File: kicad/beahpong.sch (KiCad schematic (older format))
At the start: 16 parts, among them J1 Conn_02x20_Odd_Even, J2 Conn_01x02, J3 Screw_Terminal_01x02, Q1 DMG2305UX, U1 CAT24C32, U2 DMMT5401

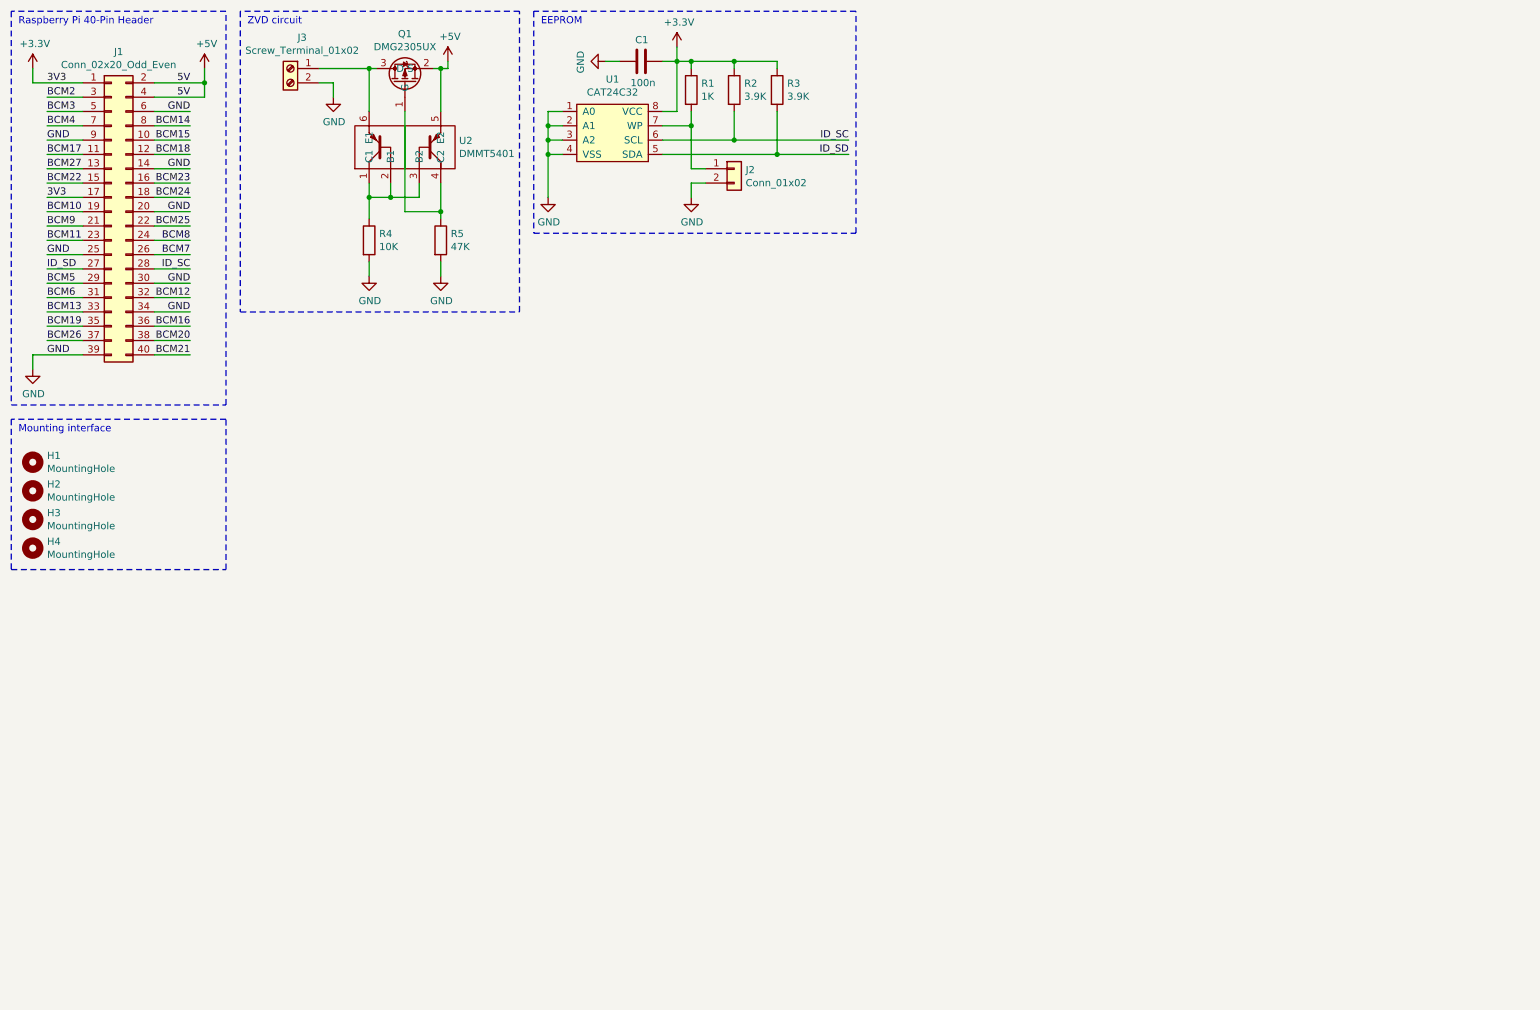
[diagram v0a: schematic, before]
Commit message: Add level shifters
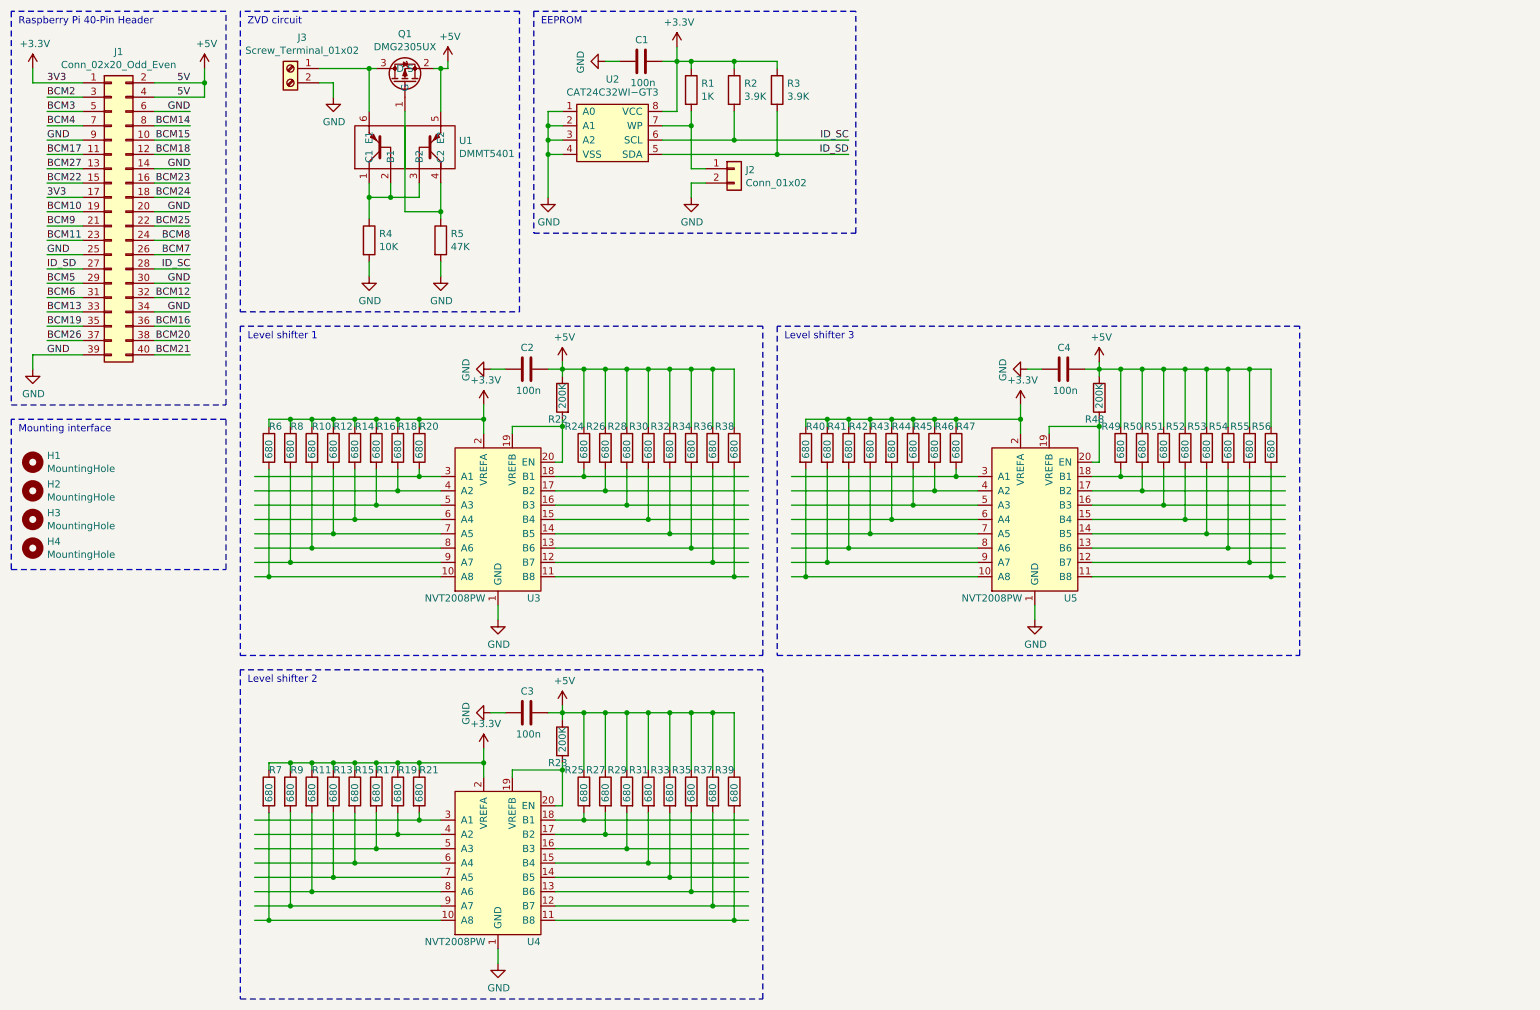
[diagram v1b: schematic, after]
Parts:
- removed U1: CAT24C32, Package_SO:SOIC-8_3.9x4.9mm_P1.27mm, symbol beahpong:CAT24C32
- removed U2: DMMT5401, Package_TO_SOT_SMD:SOT-23-6, symbol beahpong:DMMT5401
- added C2, C3, C4: 100n, Capacitor_SMD:C_0402_1005Metric, symbol Device:C
- added R10, R11, R12, R13, R14, R15, R16, R17, R18, R19, R20, R21, R24, R25, R26, R27, R28, R29, R30, R31, R32, R33, R34, R35, R36, R37, R38, R39, R40, R41, R42, R43, R44, R45, R46, R47, R49, R50, R51, R52, R53, R54, R55, R56, R6, R7, R8, R9: 680, Resistor_SMD:R_0603_1608Metric, symbol Device:R
- added R22, R23, R48: 200K, Resistor_SMD:R_0603_1608Metric, symbol Device:R
- added U1: DMMT5401, Package_TO_SOT_SMD:SOT-23-6, symbol beahpong:DMMT5401
- added U2: CAT24C32WI−GT3, Package_SO:SOIC-8_3.9x4.9mm_P1.27mm, symbol beahpong:CAT24C32WI−GT3
- added U3, U4, U5: NVT2008PW, Package_SO:TSSOP-20_4.4x6.5mm_P0.65mm, symbol beahpong:NVT2008PW
- J3: footprint Connector_Phoenix_MC:PhoenixContact_MCV_1,5_2-G-3.5_1x02_P3.50mm_Vertical -> Connector_Molex:Molex_KK-254_AE-6410-02A_1x02_P2.54mm_Vertical
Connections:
- wire segments 96 -> 372
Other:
- note added: "Level shifter 1"
- note added: "Level shifter 2"
- note added: "Level shifter 3"

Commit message: Finished layout of pcb
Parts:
- added J4, J5, J6, J7: Conn_01x03, Connector_PinHeader_2.54mm:PinHeader_1x03_P2.54mm_Vertical, symbol Connector_Generic:Conn_01x03
- added J8: Conn_02x12_Odd_Even, Connector_PinHeader_2.54mm:PinHeader_2x12_P2.54mm_Vertical, symbol Connector_Generic:Conn_02x12_Odd_Even
- J3: footprint Connector_Molex:Molex_KK-254_AE-6410-02A_1x02_P2.54mm_Vertical -> Connector_Phoenix_MC:PhoenixContact_MC_1,5_2-G-3.5_1x02_P3.50mm_Horizontal
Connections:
- net labels added: DOUT_M, DOUT_P1, DOUT_P2, RESERVED, SENSOR_P1_0, SENSOR_P1_1, SENSOR_P1_2, SENSOR_P1_3, SENSOR_P1_4, SENSOR_P1_5, SENSOR_P1_6, SENSOR_P1_7, SENSOR_P1_8, SENSOR_P1_9, SENSOR_P2_0, SENSOR_P2_1, SENSOR_P2_2, SENSOR_P2_3, SENSOR_P2_4, SENSOR_P2_5, SENSOR_P2_6, SENSOR_P2_7, SENSOR_P2_8, SENSOR_P2_9
- wire segments 372 -> 420
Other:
- note added: "Sensor header"
- note added: "WS2812B Headers"
- moved on the sheet: C2, C3, C4

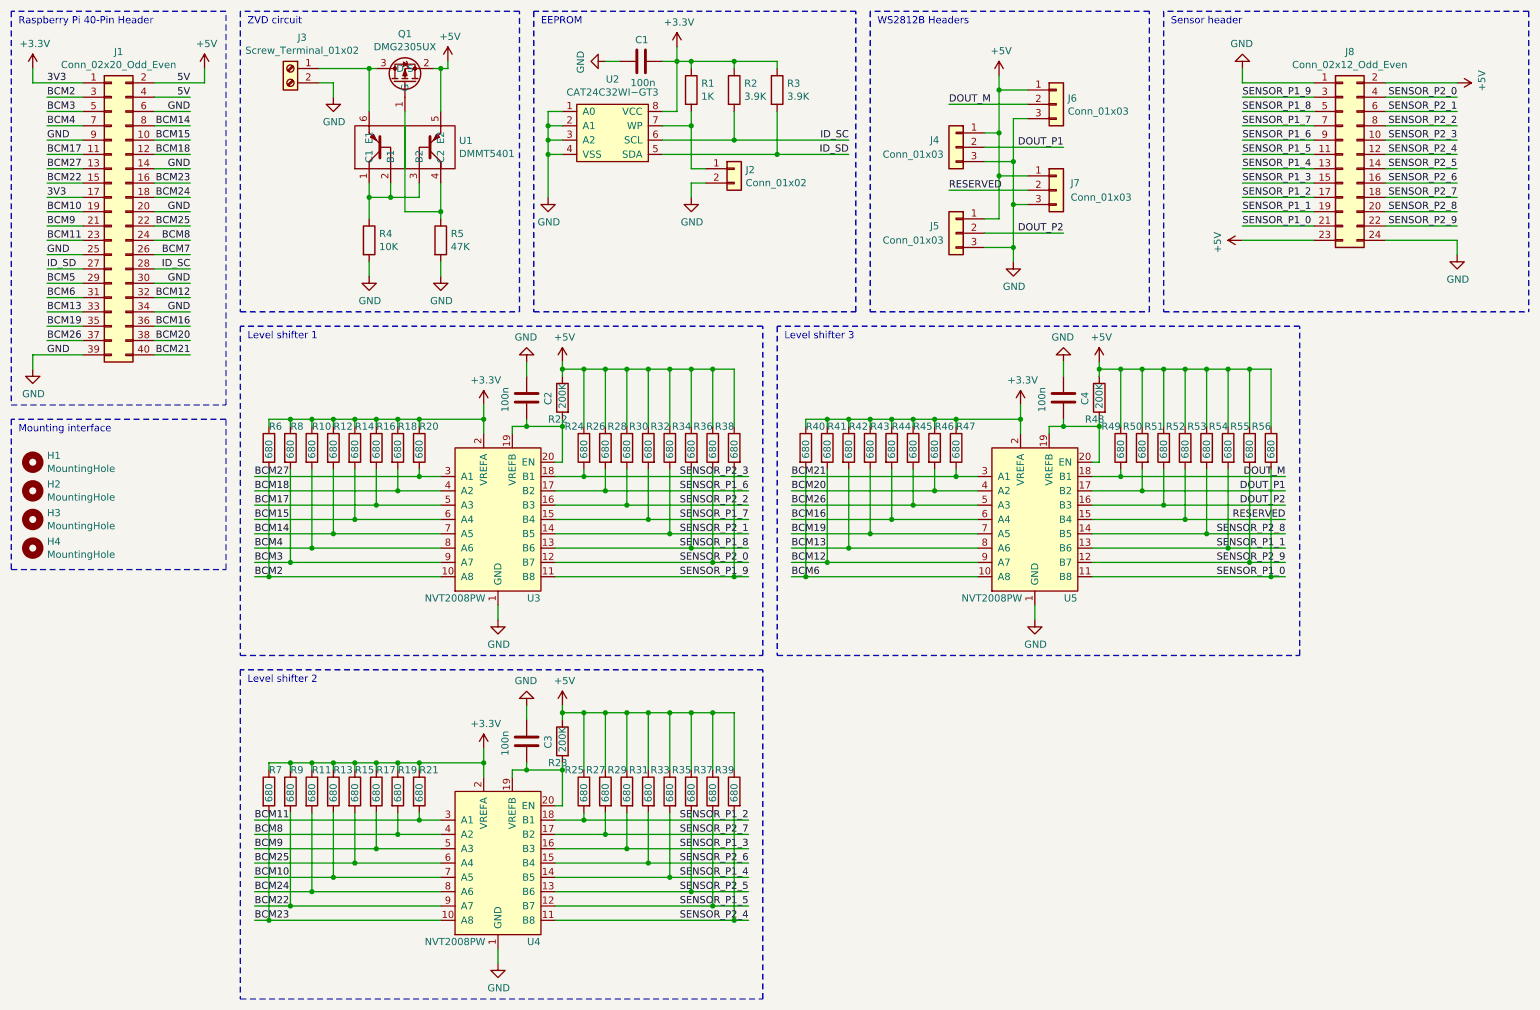
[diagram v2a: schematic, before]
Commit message: Change level shifter to one from LCSC database
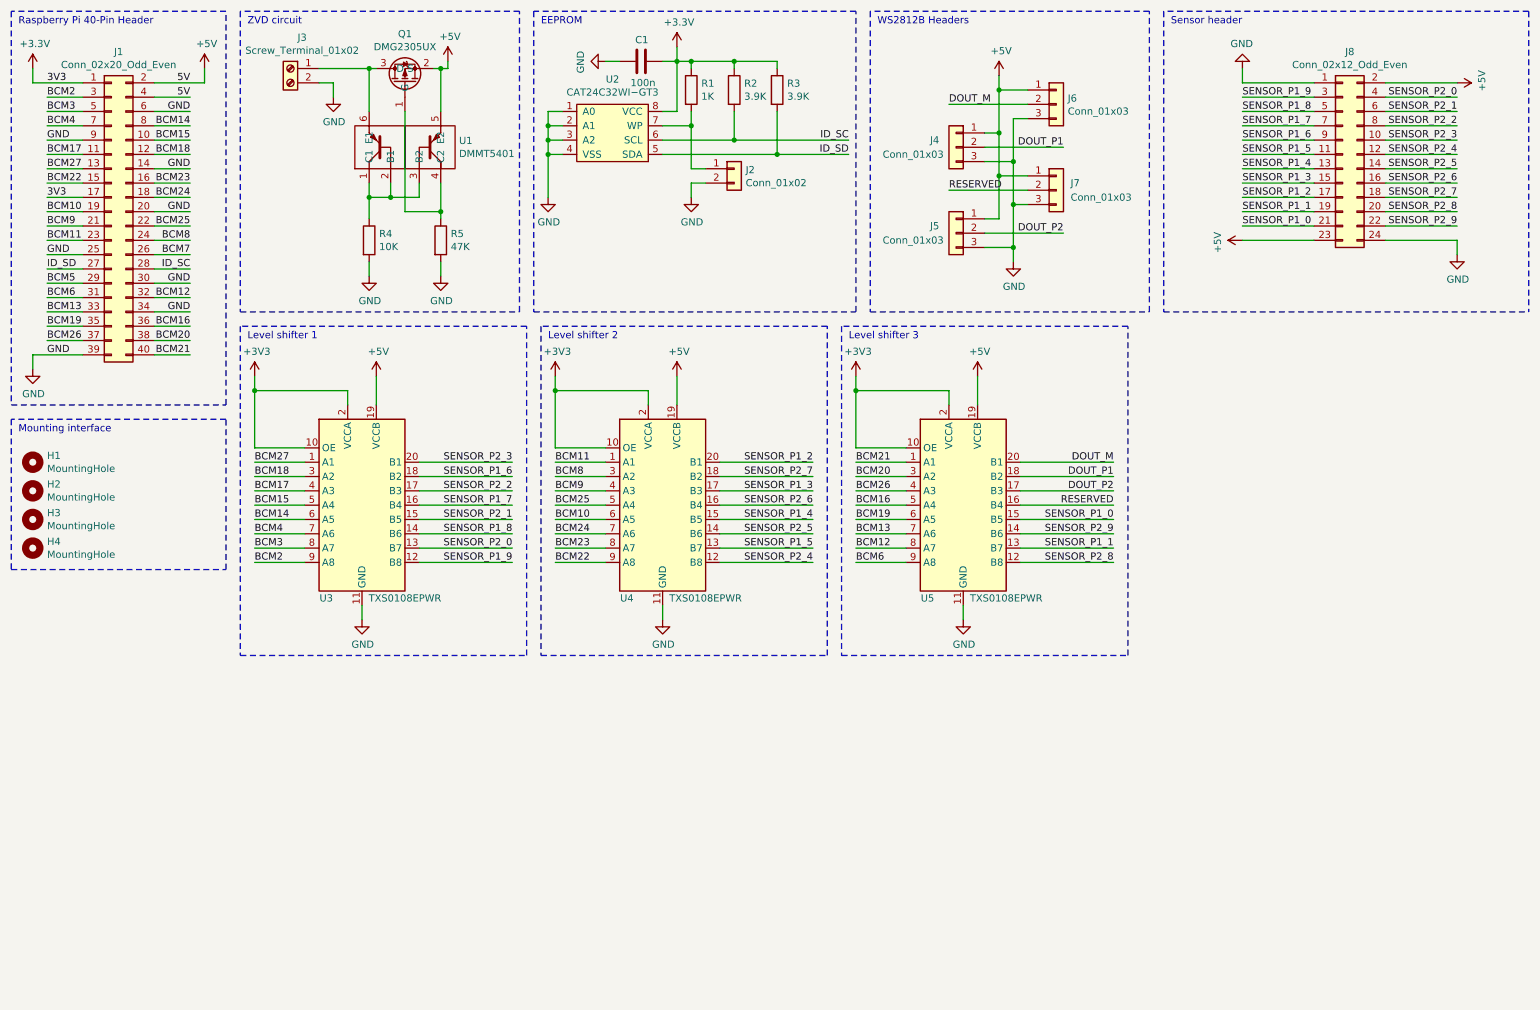
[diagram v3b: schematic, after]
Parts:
- removed C2, C3, C4: 100n, Capacitor_SMD:C_0402_1005Metric, symbol Device:C
- removed R10, R11, R12, R13, R14, R15, R16, R17, R18, R19, R20, R21, R24, R25, R26, R27, R28, R29, R30, R31, R32, R33, R34, R35, R36, R37, R38, R39, R40, R41, R42, R43, R44, R45, R46, R47, R49, R50, R51, R52, R53, R54, R55, R56, R6, R7, R8, R9: 680, Resistor_SMD:R_0603_1608Metric, symbol Device:R
- removed R22, R23, R48: 200K, Resistor_SMD:R_0603_1608Metric, symbol Device:R
- removed U3, U4, U5: NVT2008PW, Package_SO:TSSOP-20_4.4x6.5mm_P0.65mm, symbol beahpong:NVT2008PW
- added U3, U4, U5: TXS0108EPWR, Package_SO:TSSOP-20_4.4x6.5mm_P0.65mm, symbol Logic_LevelTranslator:TXS0108EPW
- C1: LCSC (none) -> C1525
- Q1: LCSC (none) -> C144153
- R1: LCSC (none) -> C11702
- R2, R3: LCSC (none) -> C51721
- R4: LCSC (none) -> C25744
- R5: LCSC (none) -> C25792
- U1: LCSC (none) -> C154733
- U2: LCSC (none) -> C81193
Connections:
- net +3V3: now also U3.10 (OE), U3.2 (VCCA), U4.10 (OE), U4.2 (VCCA), U5.10 (OE), U5.2 (VCCA)
- net +5V: now also U3.19 (VCCB), U4.19 (VCCB), U5.19 (VCCB)
- net BCM10: now also U4.6 (A5)
- net BCM11: now also U4.1 (A1)
- net BCM12: now also U5.8 (A7)
- net BCM13: now also U5.7 (A6)
- net BCM14: now also U3.6 (A5)
- net BCM15: now also U3.5 (A4)
- net BCM16: now also U5.5 (A4)
- net BCM17: now also U3.4 (A3)
- net BCM18: now also U3.3 (A2)
- net BCM19: now also U5.6 (A5)
- net BCM2: now also U3.9 (A8)
- net BCM20: now also U5.3 (A2)
- net BCM21: now also U5.1 (A1)
- net BCM22: now also U4.9 (A8)
- net BCM23: now also U4.8 (A7)
- net BCM24: now also U4.7 (A6)
- net BCM25: now also U4.5 (A4)
- net BCM26: now also U5.4 (A3)
- net BCM27: now also U3.1 (A1)
- net BCM3: now also U3.8 (A7)
- net BCM4: now also U3.7 (A6)
- net BCM6: now also U5.9 (A8)
- net BCM8: now also U4.3 (A2)
- net BCM9: now also U4.4 (A3)
- net DOUT_M: now also U5.20 (B1)
- net DOUT_P1: now also U5.18 (B2)
- net DOUT_P2: now also U5.17 (B3)
- net GND: now also U3.11 (GND), U4.11 (GND), U5.11 (GND)
- net RESERVED: now also U5.16 (B4)
- net SENSOR_P1_0: now also U5.15 (B5)
- net SENSOR_P1_1: now also U5.13 (B7)
- net SENSOR_P1_2: now also U4.20 (B1)
- net SENSOR_P1_3: now also U4.17 (B3)
- net SENSOR_P1_4: now also U4.15 (B5)
- net SENSOR_P1_5: now also U4.13 (B7)
- net SENSOR_P1_6: now also U3.18 (B2)
- net SENSOR_P1_7: now also U3.16 (B4)
- net SENSOR_P1_8: now also U3.14 (B6)
- net SENSOR_P1_9: now also U3.12 (B8)
- net SENSOR_P2_0: now also U3.13 (B7)
- net SENSOR_P2_1: now also U3.15 (B5)
- net SENSOR_P2_2: now also U3.17 (B3)
- net SENSOR_P2_3: now also U3.20 (B1)
- net SENSOR_P2_4: now also U4.12 (B8)
- net SENSOR_P2_5: now also U4.14 (B6)
- net SENSOR_P2_6: now also U4.16 (B4)
- net SENSOR_P2_7: now also U4.18 (B2)
- net SENSOR_P2_8: now also U5.12 (B8)
- net SENSOR_P2_9: now also U5.14 (B6)
